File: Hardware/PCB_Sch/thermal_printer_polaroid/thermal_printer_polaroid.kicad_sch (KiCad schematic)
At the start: 1 part

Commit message: Schematic in progress, remaining: lcd, buttons, input power
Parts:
- added C? (x6): .1 uF, symbol Device:C_Small
- added C? (x5): .01 uF, symbol Device:C_Small
- added C?: 2.2 uF, symbol Device:C_Polarized_Small_US
- added C?: 1 uF, symbol Device:C_Small
- added R?: 10 kΩ, symbol Device:R
- added R?: 1 MΩ, symbol Device:R
- added RESET_SW: SW_Push, symbol Switch:SW_Push
- added U?: ov7670_module, symbol tm4c123:ov7670_module
- added U?: thermal_printer, symbol TM4C123GH6PMI:thermal_printer
- added Y?: 8 pF, 16 MHz, symbol Device:Crystal
- gave numbers to parts that had none: 1
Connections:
- net LCD_CARD_CS: now reaches U1.10 (PD7)
- net at U1.12 (GND@1): now also U1.27 (GND@2), U1.3 (GNDA), U1.35 (GNDX), U1.39 (GND@3)
- net PRINT_TX: now reaches U1.13 (PC7)
- net PRINT_TX: now also U?. (UART_TX)
- net PRINT_RX: now reaches U1.14 (PC6)
- net PRINT_RX: now also U?. (UART_TX)
- net CAM_TX: now reaches U1.15 (PC5)
- net CAM_TX: now also U?.1 (UART_RX)
- net CAM_RX: now reaches U1.16 (PC4)
- net CAM_RX: now also U?.2 (UART_TX)
- net DEB_LED_0: now reaches U1.17 (PA0/U0RX)
- net DBG_LED_1: now reaches U1.18 (PA1/U0TX)
- net LCD_SCLK: now reaches U1.19 (PA2/SSI0CLK)
- net LCD_TFT_CS: now reaches U1.20 (PA3/SSI0FSS)
- net LCD_MISO: now reaches U1.21 (PA4/SSI0RX)
- net LCD_MOSI: now reaches U1.22 (PA5/SSI0TX)
- net LCD_D/C: now reaches U1.23 (PA6)
- net DBG_LED_7: now reaches U1.28 (PF0)
- net BUTTON_0: now reaches U1.29 (PF1)
- net BUTTON_1: now reaches U1.30 (PF2)
- net BUTTON_2: now reaches U1.31 (PF3)
- net WAKE: now reaches U1.32 (~{WAKE})
- net WAKE: now also R?.2
- net RST: now reaches U1.38 (~{RST})
- net OSC0: now reaches U1.40 (OSC0)
- net OSC0: now also C?.1, Y?.1
- net OSC1: now reaches U1.41 (OSC1)
- net OSC1: now also C?.1, Y?.2
- net DBG_LED_4: now reaches U1.43 (PD4)
- net DBG_LED_5: now reaches U1.44 (PD5)
- net TDO: now reaches U1.49 (PC3/TDO/DWO)
- net BUTTON_3: now reaches U1.5 (PF4)
- net TDI: now reaches U1.50 (PC2/TDI)
- net TMS: now reaches U1.51 (PC1/TMS/SWDIO)
- net TCK: now reaches U1.52 (PC0/TCK/SWCLK)
- net DBG_LED_6: now reaches U1.53 (PD6)
- net GND: now reaches U1.55 (GND@4)
- net GND: now also C?.2, C?.2, C?.2, C?.2, C?.2, C?.2, C?.2, C?.2, C?.2, C?.2, C?.2, C?.2, C?.2, RESET_SW.1, U?. (UART_TX), U?.0 (GND)
- net ESP8266_RX: now reaches U1.59 (PE4)
- net DBG_LED_3: now reaches U1.6 (PE3)
- net ESP8266_TX: now reaches U1.60 (PE5)
- net DBG_LED_2: now reaches U1.7 (PE2)
- new net: R?.1, RESET_SW.2
- new net +3V3: C?.1, C?.1, C?.1, C?.1, C?.1, C?.1, R?.1, R?.2
- new net +5V: U?. (UART_TX), U?.3 (5V)
- new net RESET: C?.1
- new net VDDC: C?.1, C?.1, C?.1, C?.1
- no-connect marks 0 -> 16
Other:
- removed sheet cam_interface_sch
- removed sheet printer_interface_sch
- note added: "Camera Interface"
- note added: "Printer Interface"
- note added: "SoC Oscillator/Power"
- moved on the sheet: U1

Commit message: Schematic Version 0.1
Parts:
- added C16, C18: 1 uF, symbol Device:C
- added C17, C19, C2: 4.7 uF, symbol Device:C_Polarized
- added C3: .1 uF, symbol Device:C
- added J1: USB_C_Receptacle_USB2.0, symbol Connector:USB_C_Receptacle_USB2.0
- added JP1, JP2: Jumper_2_Open, symbol Jumper:Jumper_2_Open
- added R10, R2, R4, R7, R8, R9: 10 KΩ, symbol Device:R_Small
- added R3, R5: 5.1 KΩ, symbol Device:R_Small
- added SW0: SW_UP, symbol Switch:SW_Push
- added SW1: SW_CAPTURE, symbol Switch:SW_DIP_x01
- added SW2: SW_LEFT, symbol Switch:SW_Push
- added SW3: SW_RIGHT, symbol Switch:SW_Push
- added SW4: SW_DOWN, symbol Switch:SW_Push
- added U4: ST7735_LCD, symbol TM4C123GH6PMI:ST7735_LCD
- added U5: ESP8266_BREAKOUT, symbol tm4c123:ESP8266_BREAKOUT
- added U6: UCC381DP-5G4, D8, symbol tm4c123:UCC381DP-5G4
- gave numbers to parts that had none: 18
- renumbered RESET_SW to RESET_SW1
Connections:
- net RST is gone; now on net RESET: U1.38 (~{RST})
- net +3V3: now also U1.11 (VDD@1), U1.2 (VDDA), U1.26 (VDD@2), U1.37 (VBAT), U1.42 (VDD@3), U1.54 (VDD@4), C18.1, C19.1, C2.1, C3.1, R10.1, R2.2, R4.1, R7.1, R8.1, R9.1, U4.1 (VCC), U4.9 (BACKLIGHT), U5.0 (VCC), U5.6 (GND), U6.1 (VOUT), U6.4 (VOUTS)
- net +5V: now also C16.1, C17.1, JP1.2 (B), U6.8 (VIN)
- net ESP8266_RX: now also U1.60 (PE5), U5.1 (UART_RX); no longer U1.59 (PE4)
- net ESP8266_TX: now also U1.59 (PE4), U5.2 (UART_TX); no longer U1.60 (PE5)
- net GND: now also U1.12 (GND@1), U1.27 (GND@2), U1.3 (GNDA), U1.34 (XOSC0), U1.35 (GNDX), U1.39 (GND@3), C16.2, C17.2, C18.2, C19.2, C2.2, C3.2, J1.A1 (GND), J1.A12 (GND), J1.B1 (GND), J1.B12 (GND), J1.S1 (SHIELD), JP2.1 (A), R3.2, R5.2, SW0.1, SW1.1, SW2.1, SW3.1, SW4.1, U4.0 (GND), U6.2 (GND), U6.3 (GND), U6.6 (GND), U6.7 (GND)
- net LCD_CARD_CS: now also U4.4 (CARD_CS)
- net LCD_D/C: now also U4.3 (DATA/COMMAND)
- net LCD_MISO: now also U4.8 (MISO)
- net LCD_MOSI: now also U4.6 (MOSI)
- net LCD_RST: now also U1.24 (PA7), U4.2 (RESET)
- net LCD_SCLK: now also U4.7 (SCLK)
- net LCD_TFT_CS: now also U4.5 (TFT_CS)
- net VDDC: now also U1.25 (VDDC@1), U1.56 (VDDC@2)
- net ESP8266_IO2: now reaches U1.8 (PE1)
- net ESP8266_IO2: now also U5.5 (IO2)
- net ESP8266_RESET: now reaches U1.9 (PE0)
- net ESP8266_RESET: now also U5.3 (RESET)
- net BUTTON_0 renamed BUTTON_U
- net BUTTON_U: now also R7.2, SW0.2
- net BUTTON_1 renamed BUTTON_L
- net BUTTON_L: now also R8.2, SW2.2
- net BUTTON_2 renamed BUTTON_R
- net BUTTON_R: now also R9.2, SW3.2
- net BUTTON_3 renamed BUTTON_D
- net BUTTON_D: now also R10.2, SW4.2
- net DBG_LED_7 renamed BUTTON_C
- net BUTTON_C: now also R4.2, SW1.2
- new net: JP2.2 (B), U6.5 (CT)
- new net: J1.A4 (VBUS), J1.A9 (VBUS), J1.B4 (VBUS), J1.B9 (VBUS), JP1.1 (A)
- new net: R2.1, U5.4 (IO0)
- new net: J1.A5 (CC1), R5.1
- new net: J1.B5 (CC2), R3.1
- no-connect marks 16 -> 20
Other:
- removed sheet button_interface_sch
- removed sheet esp8266_interface
- removed sheet lcd_interface_sch
- note added: "Button Interface"
- note added: "LCD/SD Card Interface"
- note added: "Power 3.3V"
- note added: "Power Input"
- note added: "TM4C123 Oscillator/Power"
- note added: "WIFI Interface"
- note removed: "SoC Oscillator/Power"
- moved on the sheet: C1, C10, C11, C12, C13, C14, C15, C4, C5, C6, C7, C8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

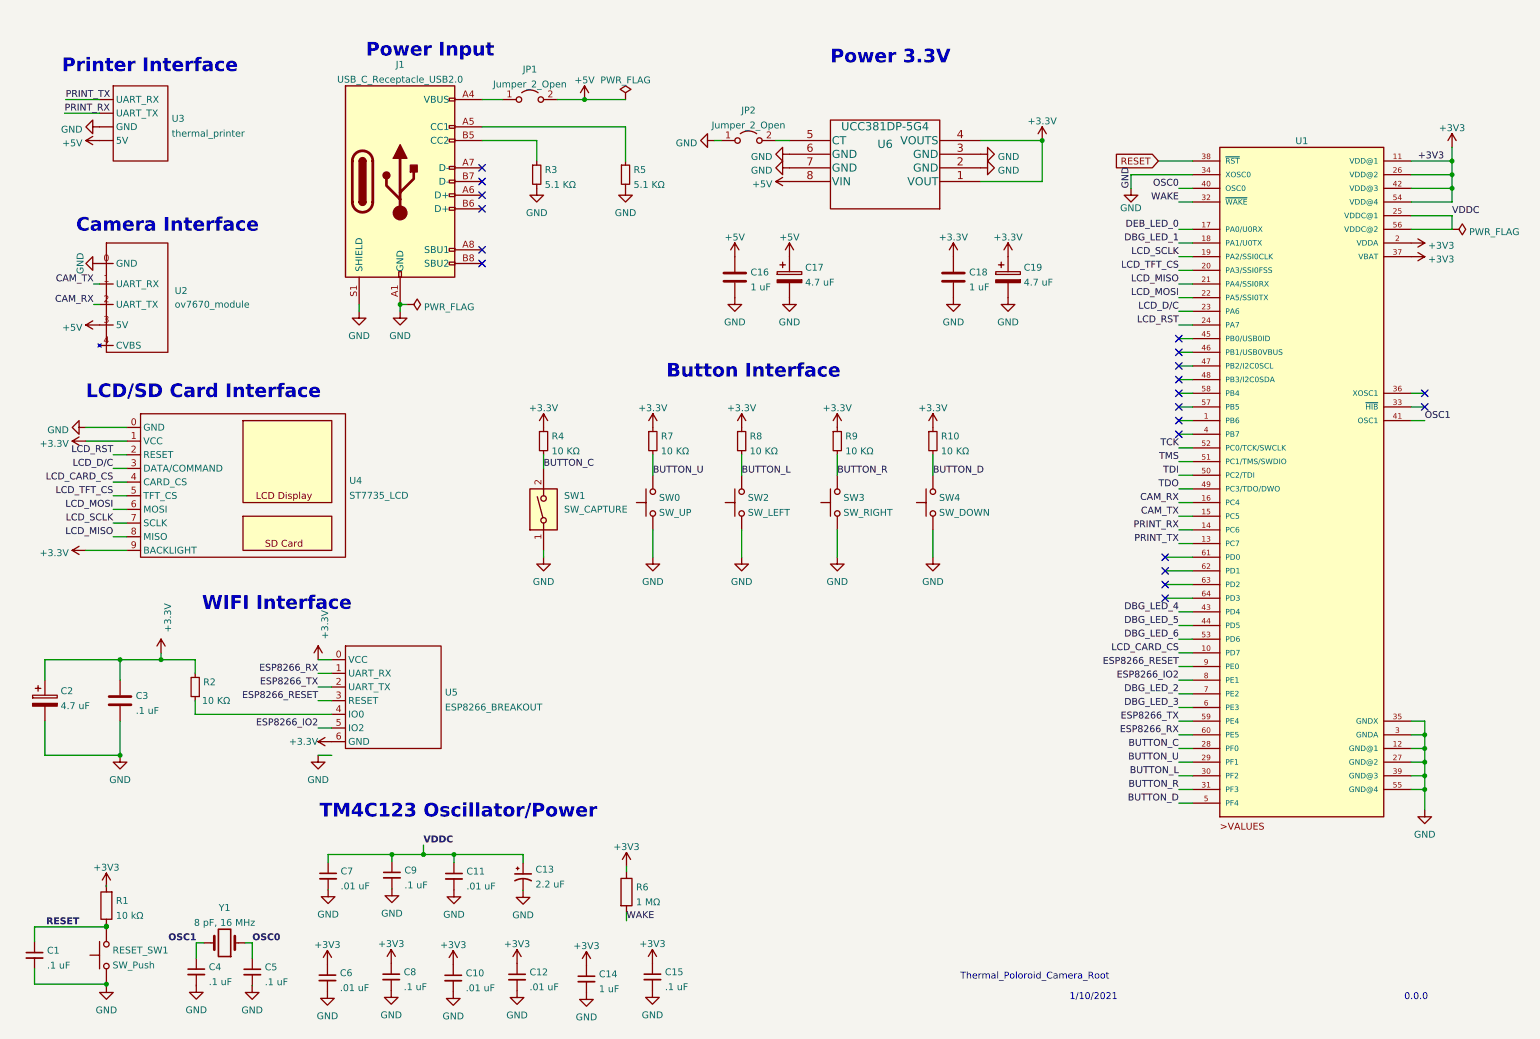
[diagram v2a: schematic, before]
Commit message: Update schematic to mostly have footprints assigned
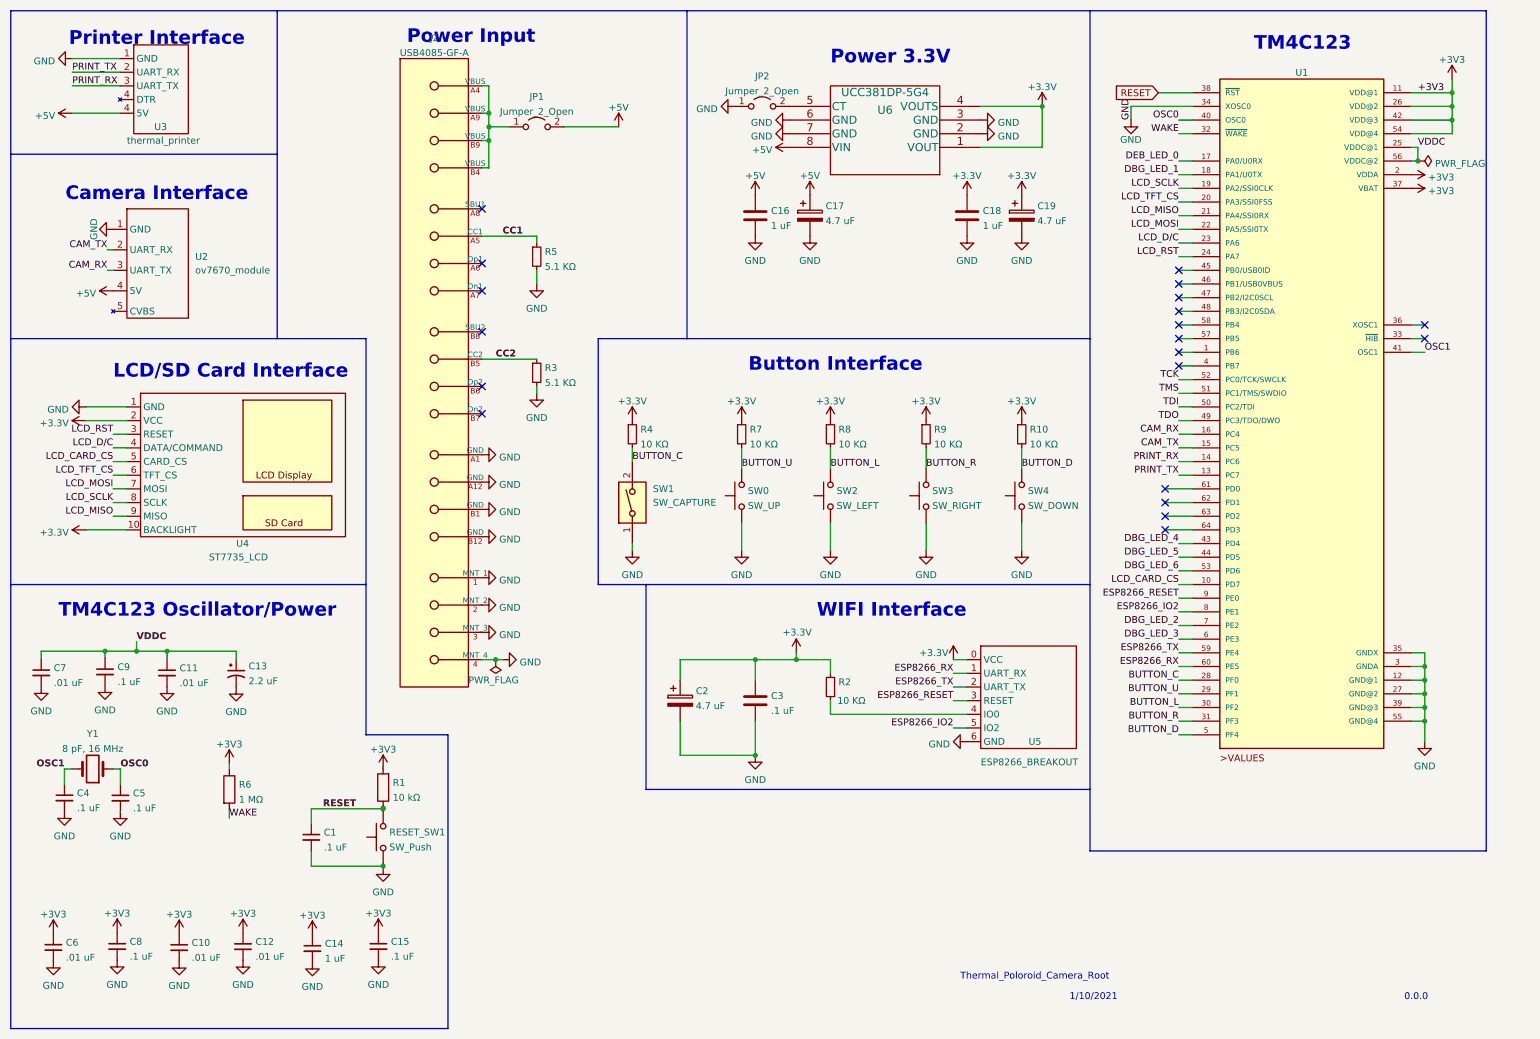
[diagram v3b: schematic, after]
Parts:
- removed J1: USB_C_Receptacle_USB2.0, symbol Connector:USB_C_Receptacle_USB2.0
- added J2: USB4085-GF-A, Connector_USB:USB_C_Receptacle_GCT_USB4085, symbol tm4c123:USB4085-GF-A
- C1, C10, C11, C12, C13, C14, C15, C16, C17, C18, C19, C2, C3, C4, C5, C6, C7, C8, C9: footprint (none) -> Capacitor_SMD:C_0805_2012Metric
- JP1, JP2, RESET_SW1: footprint (none) -> Connector_PinHeader_2.54mm:PinHeader_1x02_P2.54mm_Vertical
- R1, R10, R2, R3, R4, R5, R6, R7, R8, R9: footprint (none) -> Resistor_SMD:R_0805_2012Metric_Pad1.20x1.40mm_HandSolder
- U2, U3: footprint (none) -> Connector_PinHeader_2.54mm:PinHeader_1x05_P2.54mm_Vertical
- U4: footprint (none) -> Connector_PinHeader_2.54mm:PinHeader_1x10_P2.54mm_Vertical
- Y1: footprint (none) -> Crystal:Crystal_HC49-4H_Vertical
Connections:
- net +3V3: now also U4.10 (BACKLIGHT), U4.2 (VCC); no longer U4.1 (VCC), U4.9 (BACKLIGHT), U5.6 (GND)
- net +5V: now also U2.4 (5V), U3.4 (DTR); no longer U2.3 (5V), U3. (UART_TX)
- net CAM_RX: now also U2.3 (UART_TX); no longer U2.2 (UART_TX)
- net CAM_TX: now also U2.2 (UART_RX); no longer U2.1 (UART_RX)
- net GND: now also U2.1 (GND), U3.1 (GND), U4.1 (GND), U5.6 (GND), J2.1 (MNT_1), J2.2 (MNT_2), J2.3 (MNT_3), J2.4 (MNT_4), J2.A1 (GND), J2.A12 (GND), J2.B1 (GND), J2.B12 (GND); no longer U2.0 (GND), U3. (UART_TX), U4.0 (GND)
- net LCD_CARD_CS: now also U4.5 (CARD_CS); no longer U4.4 (CARD_CS)
- net LCD_D/C: now also U4.4 (DATA/COMMAND); no longer U4.3 (DATA/COMMAND)
- net LCD_MISO: now also U4.9 (MISO); no longer U4.8 (MISO)
- net LCD_MOSI: now also U4.7 (MOSI); no longer U4.6 (MOSI)
- net LCD_RST: now also U4.3 (RESET); no longer U4.2 (RESET)
- net LCD_SCLK: now also U4.8 (SCLK); no longer U4.7 (SCLK)
- net LCD_TFT_CS: now also U4.6 (TFT_CS); no longer U4.5 (TFT_CS)
- net PRINT_RX: now also U3.3 (UART_TX); no longer U3. (UART_TX)
- net PRINT_TX: now also U3.2 (UART_RX); no longer U3. (UART_TX)
- net at JP1.1 (A): now also J2.A4 (VBUS), J2.A9 (VBUS), J2.B4 (VBUS), J2.B9 (VBUS)
- net CC1: now reaches R5.1
- net CC1: now also J2.A5 (CC1)
- net CC2: now reaches R3.1
- net CC2: now also J2.B5 (CC2)
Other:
- note added: "TM4C123"
- moved on the sheet: C1, C10, C11, C12, C13, C14, C15, C16, C17, C18, C19, C2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
